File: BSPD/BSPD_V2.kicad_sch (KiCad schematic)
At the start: 33 parts, among them J2 Conn_01x02_Socket, J3 Conn_01x02_Socket, J4 Conn_01x02_Socket, K1 Fujitsu_FTR-LYCA005x, Q1 NMOS, Q2 NMOS, Q3 NMOS, U1 CD4001BM, U2 CD4001BM, U3 LM393, U5 LM393

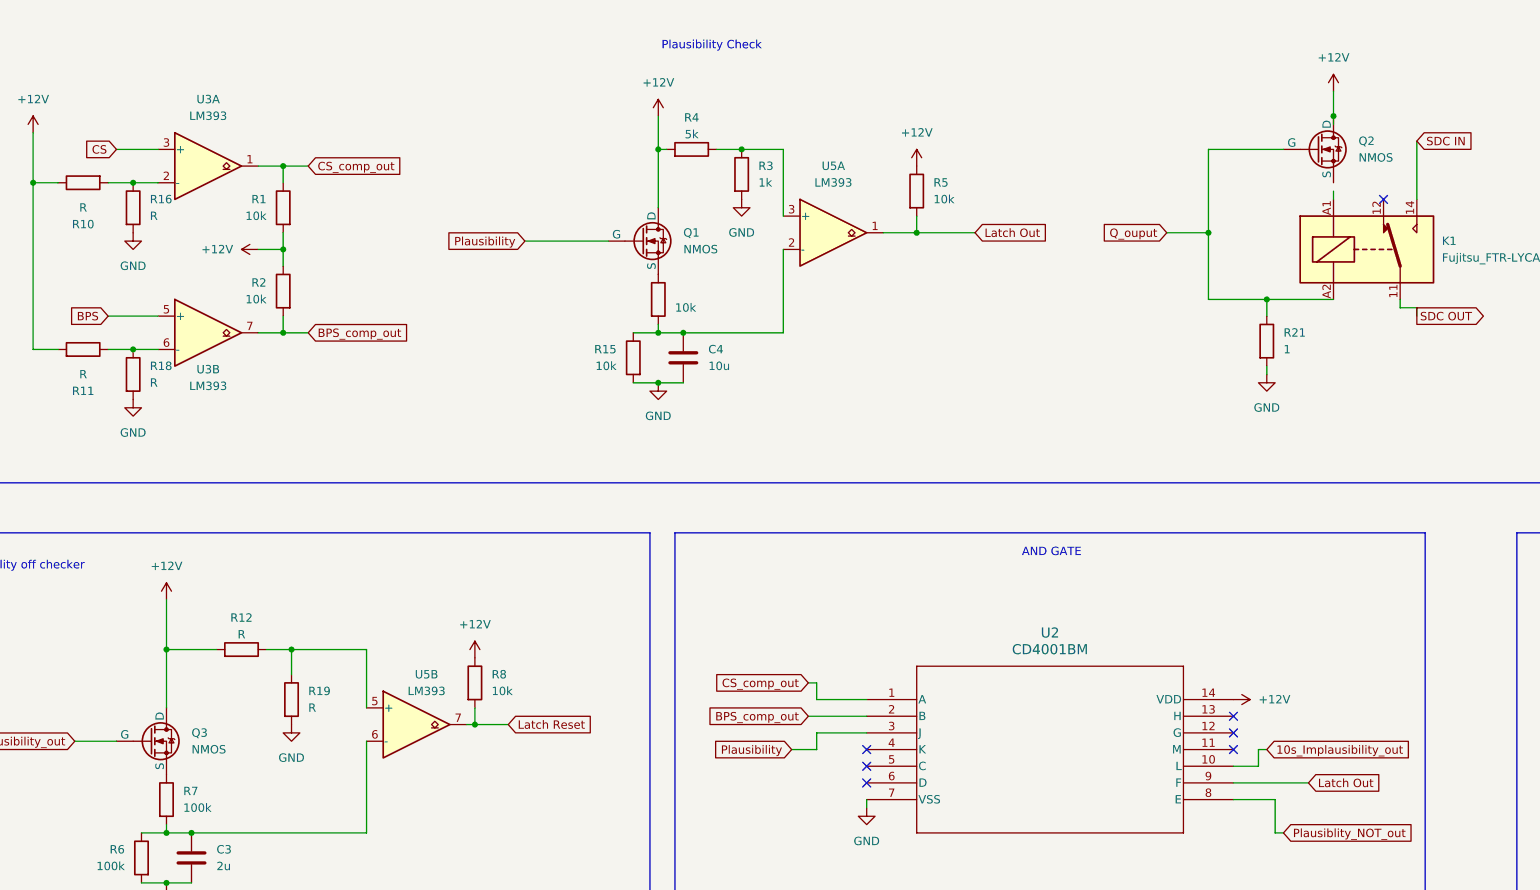
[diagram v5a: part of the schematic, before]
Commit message: Added AO3400A as the switching mosfets everywhere, decent rds of 25.6 m ohm at 10V Vgs, but we are using 12V so that's a bit better. 34 inr, and 30V Vds max, helps in not destroying the mosfet when directly powered from the GLV
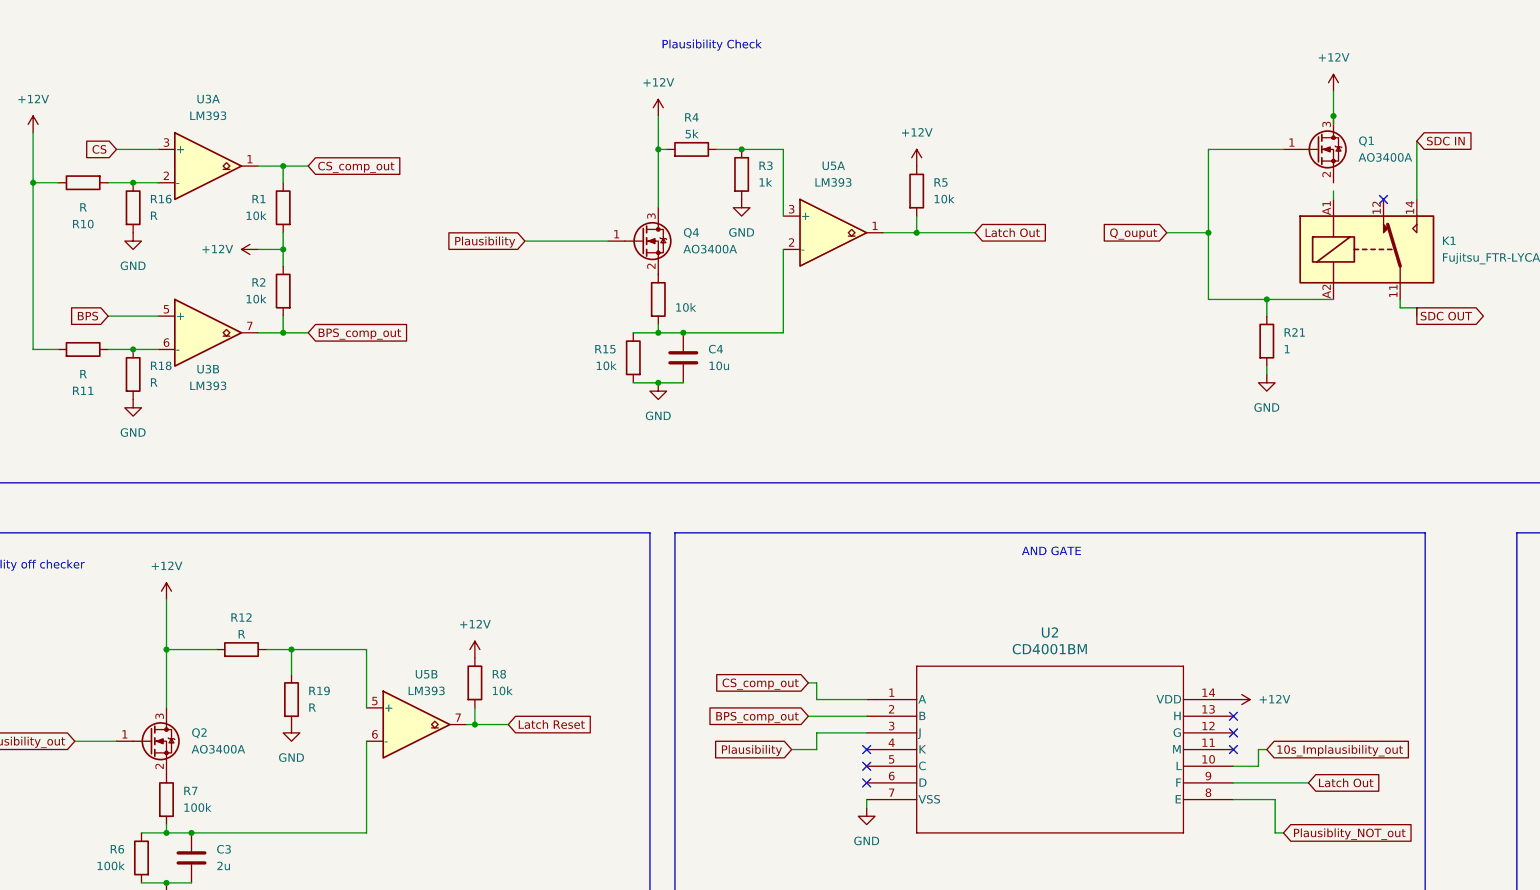
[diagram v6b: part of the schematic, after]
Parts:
- removed Q1, Q2, Q3: NMOS, symbol Simulation_SPICE:NMOS
- added Q1, Q2, Q4: AO3400A, Package_TO_SOT_SMD:SOT-23, symbol Transistor_FET:AO3400A
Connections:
- net +12V: now also Q1.3 (D), Q2.3 (D), Q4.3 (D)
- net 10s_Implausibility_out: now also Q2.1 (G)
- net Plausibility: now also Q4.1 (G)
- net Q_ouput: now also Q1.1 (G)
- net at R7.1: now also Q2.2 (S)
- net at R14.1: now also Q4.2 (S)

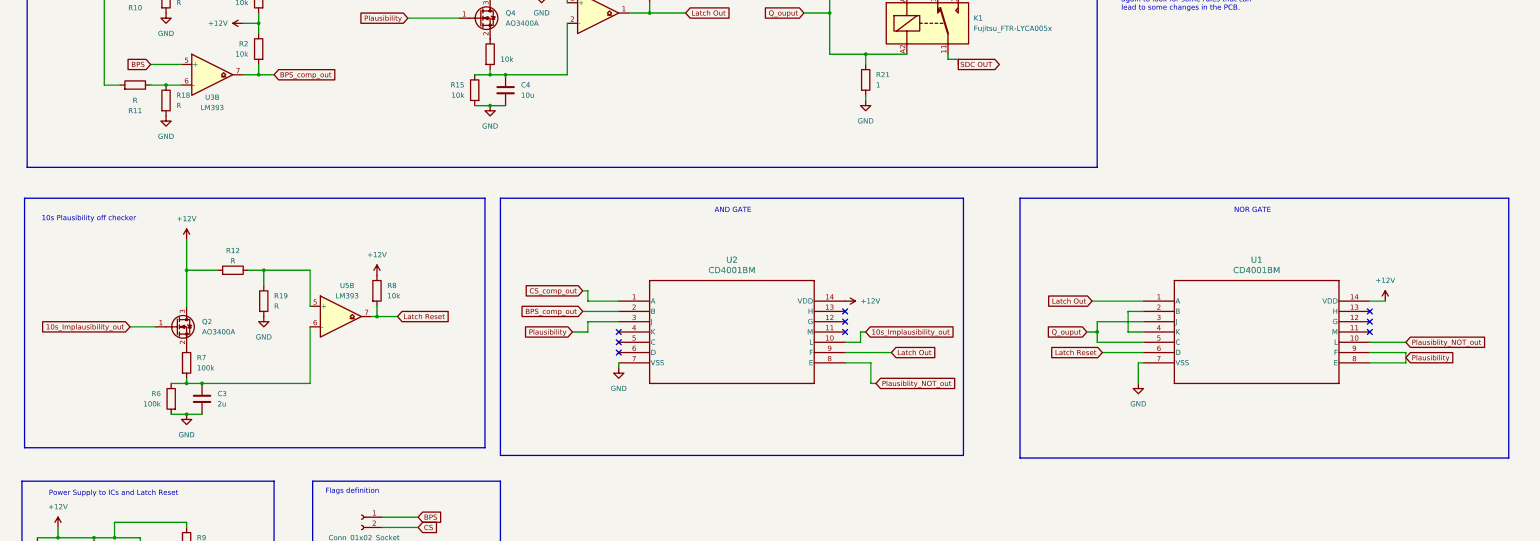
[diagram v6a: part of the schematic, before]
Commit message: Added the NPN transistor logic to instantly discharge the capacitor irrespective of the charge it holds. This logic is verified in LTSpice and has helped in removing the discharging resistor, reducing calculation complexity(somewhat). Also didn't have to use any extra external ic :)
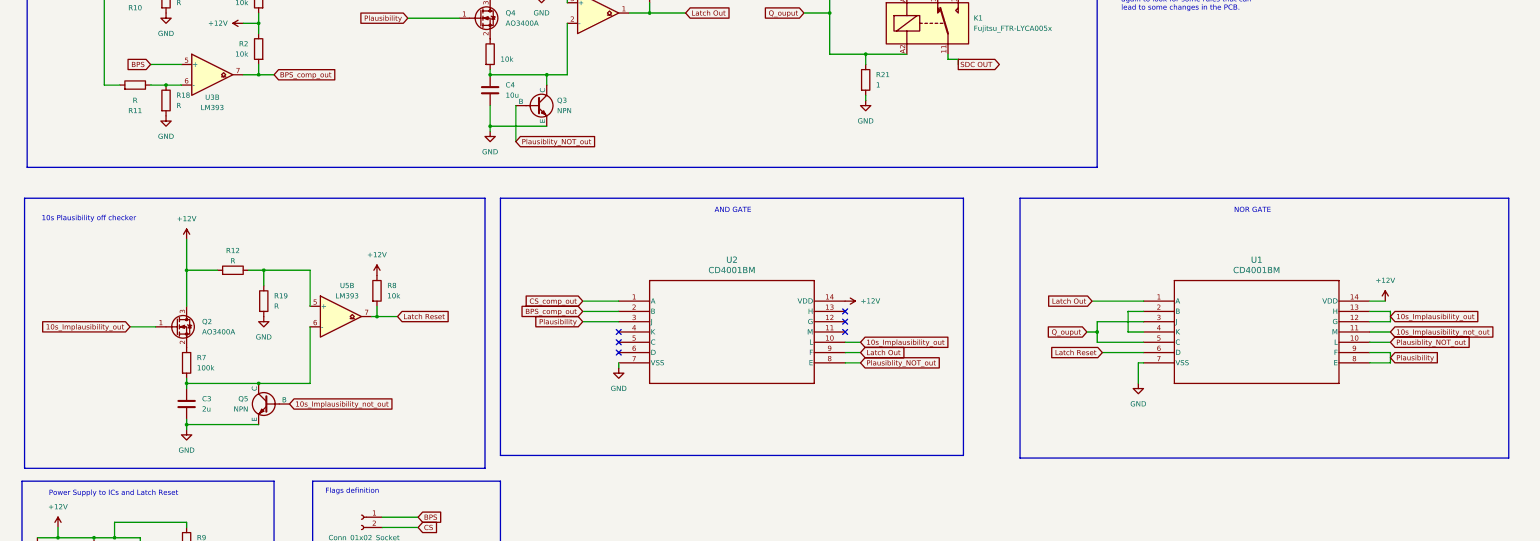
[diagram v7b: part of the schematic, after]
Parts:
- removed R15: 10k, symbol Device:R
- removed R6: 100k, symbol Device:R
- added Q3, Q5: NPN, symbol Simulation_SPICE:NPN
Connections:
- net 10s_Implausibility_out: now also U1.12 (G), U1.13 (H)
- net GND: now also Q3.3 (E), Q5.3 (E)
- net Plausiblity_NOT_out: now also Q3.2 (B)
- net at C3.1, R7.2, U5.6 (-): now also Q5.1 (C)
- net at C4.1, R14.2, U5.2 (-): now also Q3.1 (C)
- net 10s_Implausibility_not_out: now reaches U1.11 (M)
- net 10s_Implausibility_not_out: now also Q5.2 (B)
- no-connect marks 10 -> 7
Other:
- moved on the sheet: C3, C4
